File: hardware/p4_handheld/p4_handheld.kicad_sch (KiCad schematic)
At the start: 0 parts

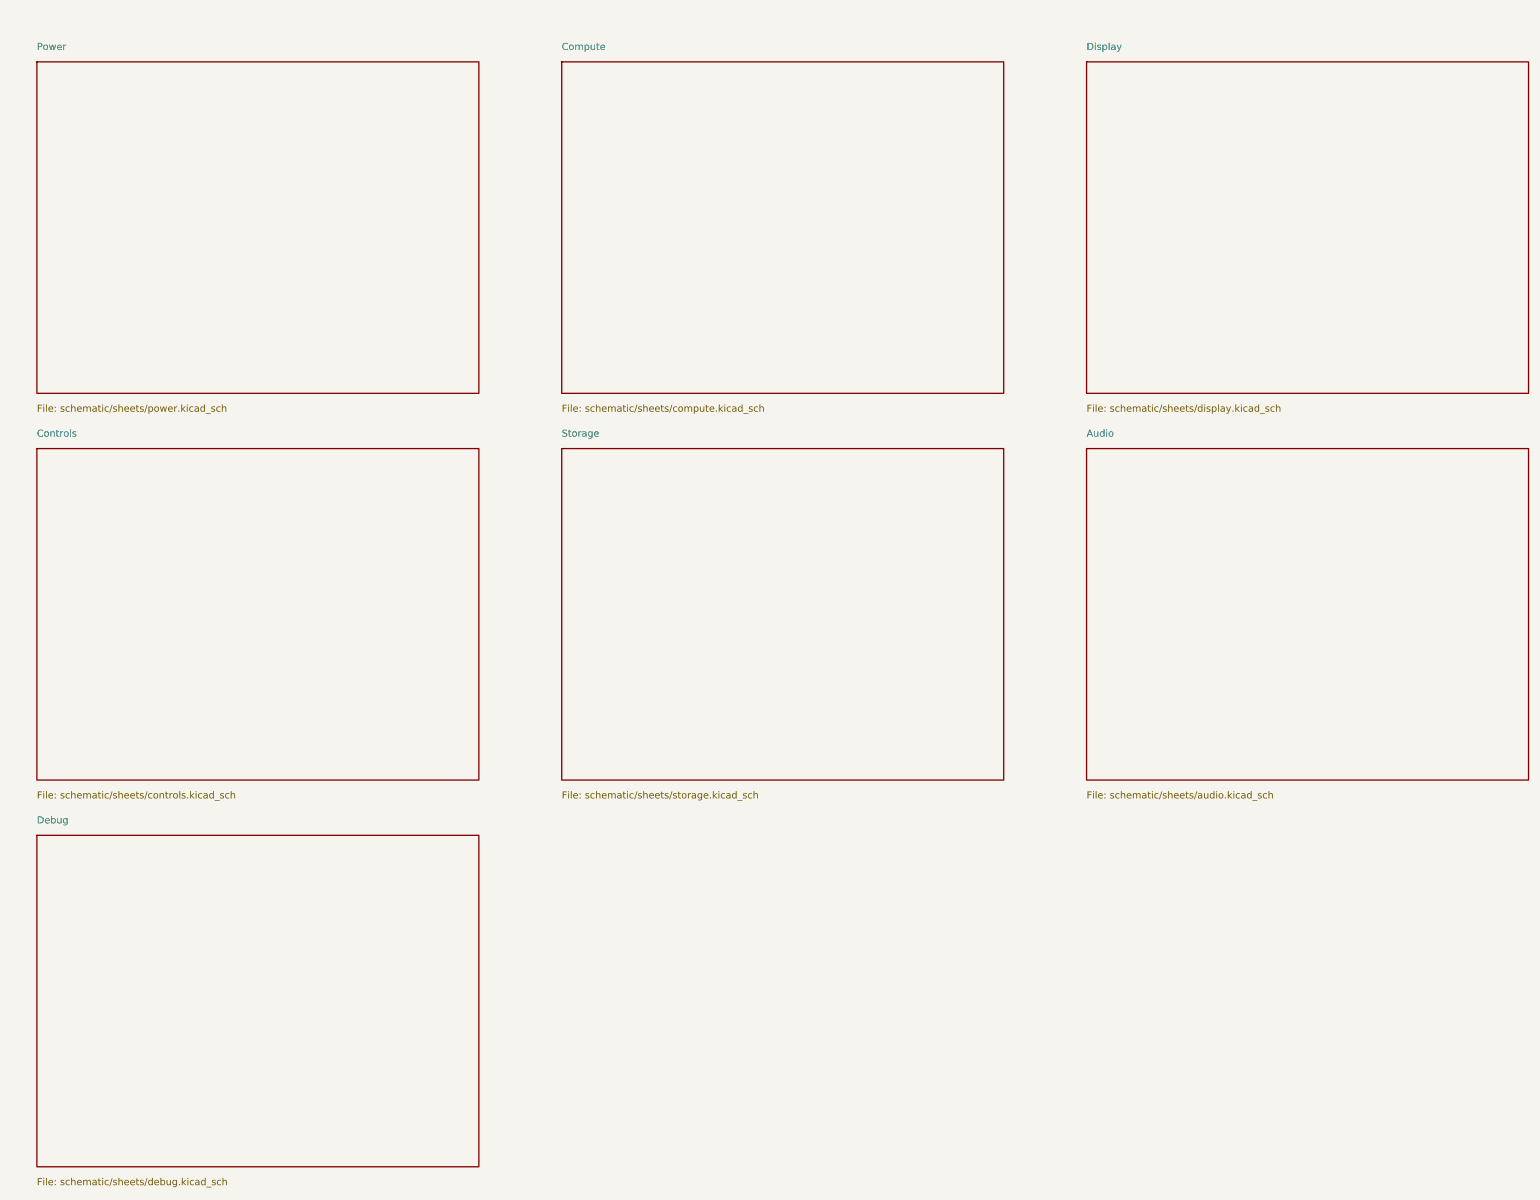
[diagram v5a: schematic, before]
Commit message: hw(p4_handheld): ERC-clean schematic engine (real pins, on-endpoint labels, project symbol lib)
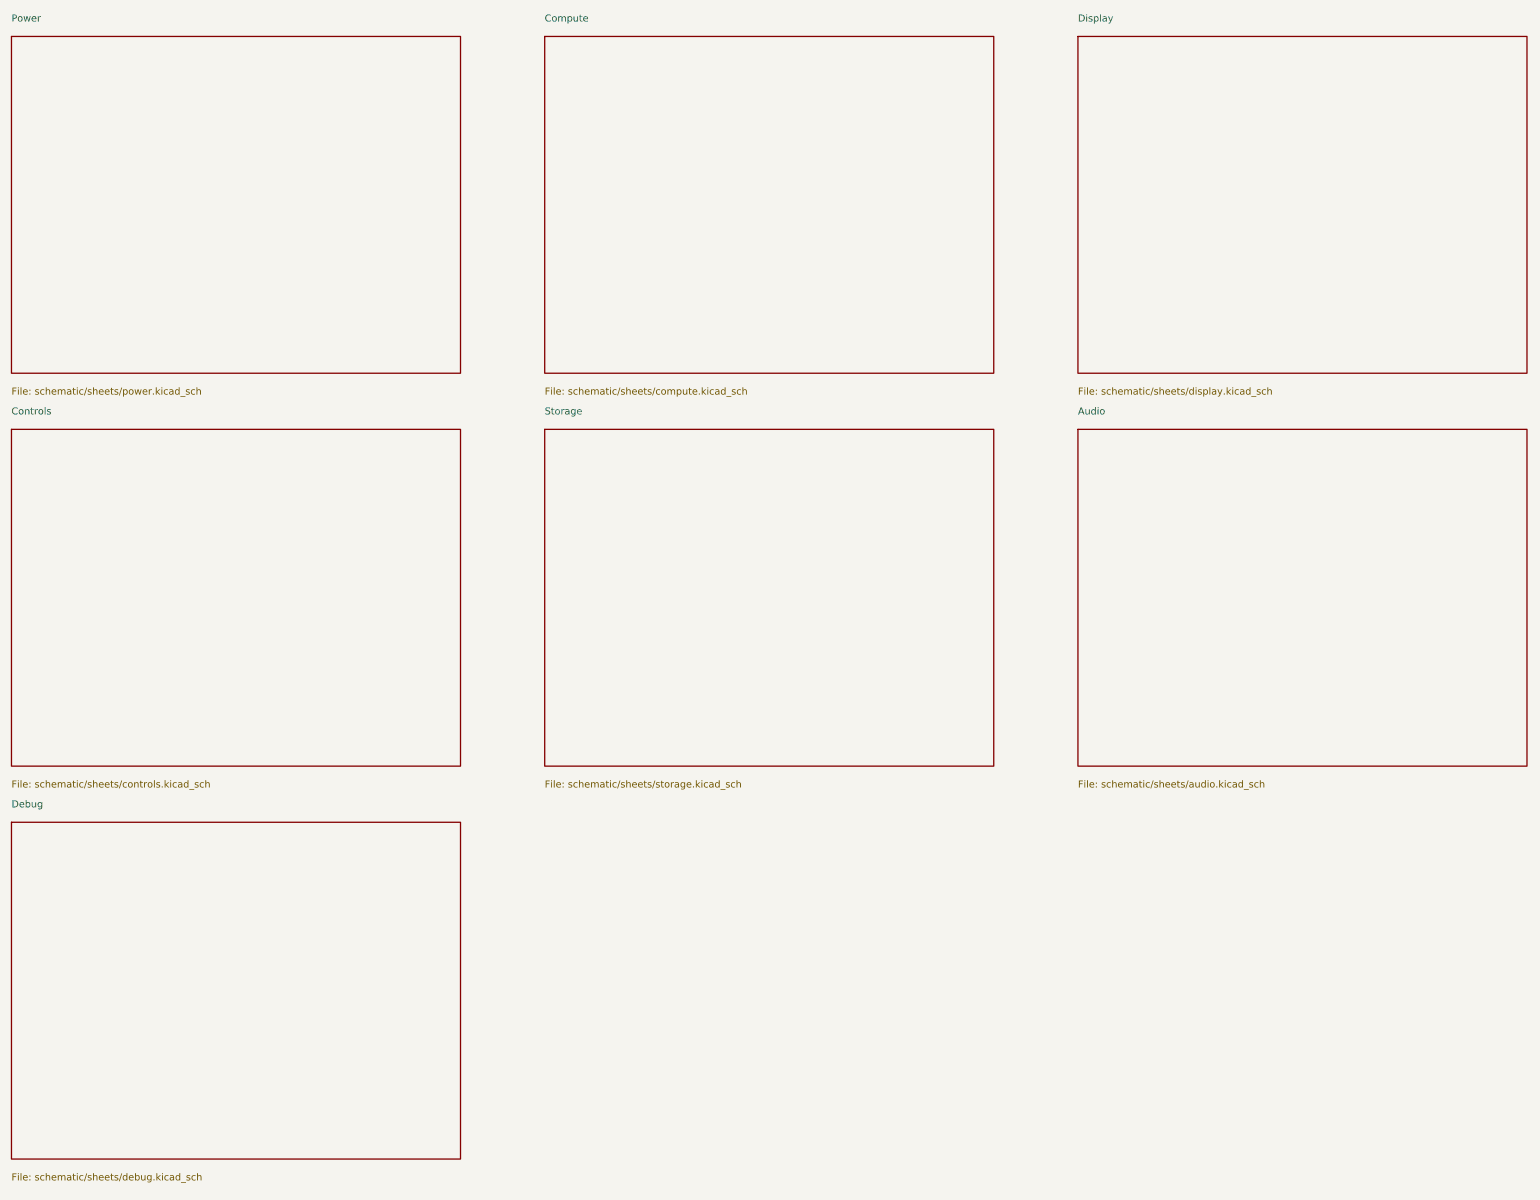
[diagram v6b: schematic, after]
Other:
- title: PuzzleScript Card -> PuzzleScript P4 Handheld
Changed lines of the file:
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@@
   (paper "A3")
   (title_block
-    (title "PuzzleScript Card")
+    (title "PuzzleScript P4 Handheld")
     (date "2026-07-12")
-    (rev "spin1")
+    (rev "circuit-phase-0")
   )
-  (sheet (at 30 30) (size 80 60) (fields_autoplaced)
+  (sheet (at 25.4 25.4) (size 81.28 60.96) (fields_autoplaced)
     (stroke (width 0.1524) (type solid)) (fill (type none))
-    (property "Sheetname" "Power" (at 30 28 0)
+    (property "Sheetname" "Power" (at 25.4 22.86 0)
       (effects (font (size 1.27 1.27)) (justify left bottom)))
-    (property "Sheetfile" "schematic/sheets/power.kicad_sch" (at 30 92 0)
+    (property "Sheetfile" "schematic/sheets/power.kicad_sch" (at 25.4 88.9 0)
       (effects (font (size 1.27 1.27)) (justify left top)))
   )
-  (sheet (at 125 30) (size 80 60) (fields_autoplaced)
+  (sheet (at 121.92 25.4) (size 81.28 60.96) (fields_autoplaced)
     (stroke (width 0.1524) (type solid)) (fill (type none))
-    (property "Sheetname" "Compute" (at 125 28 0)
+    (property "Sheetname" "Compute" (at 121.92 22.86 0)
       (effects (font (size 1.27 1.27)) (justify left bottom)))
-    (property "Sheetfile" "schematic/sheets/compute.kicad_sch" (at 125 92 0)
+    (property "Sheetfile" "schematic/sheets/compute.kicad_sch" (at 121.92 88.9 0)
       (effects (font (size 1.27 1.27)) (justify left top)))
   )
-  (sheet (at 220 30) (size 80 60) (fields_autoplaced)
+  (sheet (at 218.44 25.4) (size 81.28 60.96) (fields_autoplaced)
     (stroke (width 0.1524) (type solid)) (fill (type none))
-    (property "Sheetname" "Display" (at 220 28 0)
+    (property "Sheetname" "Display" (at 218.44 22.86 0)
       (effects (font (size 1.27 1.27)) (justify left bottom)))
-    (property "Sheetfile" "schematic/sheets/display.kicad_sch" (at 220 92 0)
+    (property "Sheetfile" "schematic/sheets/display.kicad_sch" (at 218.44 88.9 0)
       (effects (font (size 1.27 1.27)) (justify left top)))
   )
-  (sheet (at 30 100) (size 80 60) (fields_autoplaced)
+  (sheet (at 25.4 96.52) (size 81.28 60.96) (fields_autoplaced)
     (stroke (width 0.1524) (type solid)) (fill (type none))
-    (property "Sheetname" "Controls" (at 30 98 0)
+    (property "Sheetname" "Controls" (at 25.4 93.98 0)
       (effects (font (size 1.27 1.27)) (justify left bottom)))
-    (property "Sheetfile" "schematic/sheets/controls.kicad_sch" (at 30 162 0)
+    (property "Sheetfile" "schematic/sheets/controls.kicad_sch" (at 25.4 160.02 0)
       (effects (font (size 1.27 1.27)) (justify left top)))
   )
-  (sheet (at 125 100) (size 80 60) (fields_autoplaced)
+  (sheet (at 121.92 96.52) (size 81.28 60.96) (fields_autoplaced)
     (stroke (width 0.1524) (type solid)) (fill (type none))
-    (property "Sheetname" "Storage" (at 125 98 0)
+    (property "Sheetname" "Storage" (at 121.92 93.98 0)
       (effects (font (size 1.27 1.27)) (justify left bottom)))
-    (property "Sheetfile" "schematic/sheets/storage.kicad_sch" (at 125 162 0)
+    (property "Sheetfile" "schematic/sheets/storage.kicad_sch" (at 121.92 160.02 0)
       (effects (font (size 1.27 1.27)) (justify left top)))
   )
-  (sheet (at 220 100) (size 80 60) (fields_autoplaced)
+  (sheet (at 218.44 96.52) (size 81.28 60.96) (fields_autoplaced)
     (stroke (width 0.1524) (type solid)) (fill (type none))
-    (property "Sheetname" "Audio" (at 220 98 0)
+    (property "Sheetname" "Audio" (at 218.44 93.98 0)
       (effects (font (size 1.27 1.27)) (justify left bottom)))
-    (property "Sheetfile" "schematic/sheets/audio.kicad_sch" (at 220 162 0)
+    (property "Sheetfile" "schematic/sheets/audio.kicad_sch" (at 218.44 160.02 0)
       (effects (font (size 1.27 1.27)) (justify left top)))
   )
-  (sheet (at 30 170) (size 80 60) (fields_autoplaced)
+  (sheet (at 25.4 167.64) (size 81.28 60.96) (fields_autoplaced)
     (stroke (width 0.1524) (type solid)) (fill (type none))
-    (property "Sheetname" "Debug" (at 30 168 0)
+    (property "Sheetname" "Debug" (at 25.4 165.1 0)
       (effects (font (size 1.27 1.27)) (justify left bottom)))
-    (property "Sheetfile" "schematic/sheets/debug.kicad_sch" (at 30 232 0)
+    (property "Sheetfile" "schematic/sheets/debug.kicad_sch" (at 25.4 231.14 0)
       (effects (font (size 1.27 1.27)) (justify left top)))
   )
